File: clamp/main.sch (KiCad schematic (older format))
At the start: 36 parts, among them P1 CONN_01X12, U1 LM741, U2 LM741, U3 LM741, U4 LM741, U5 LM741, U6 LM741

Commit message: update
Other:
- moved on the sheet: R3, R4, R5
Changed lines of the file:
@@
 	4750 2250 4900 2250
+Wire Wire Line
+	4250 1850 4250 2050
 Wire Wire Line
 	4050 2050 4900 2050
@@
 Text GLabel 7550 4500 0    60   Input ~ 0
 -VE
-Text GLabel 1550 2050 0    60   Input ~ 0
+Text GLabel 1550 1850 0    60   Input ~ 0
 I-FB
 Text GLabel 1500 1500 0    60   Input ~ 0
 REF
-Text GLabel 1550 2250 0    60   Input ~ 0
+Text GLabel 1550 2050 0    60   Input ~ 0
 I-SET
 $Comp
 L R R3
 U 1 1 5807AAE8
+P 3900 1850
+F 0 "R3" V 3980 1850 50  0000 C CNN
+F 1 "R" V 3900 1850 50  0000 C CNN
+F 2 "Resistors_SMD:R_1206" V 3830 1850 50  0001 C CNN
+F 3 "" H 3900 1850 50  0000 C CNN
+	1    3900 1850
+	0    1    1    0
+$EndComp
+$Comp
+L R R4
+U 1 1 5807AB49
 P 3900 2050
-F 0 "R3" V 3980 2050 50  0000 C CNN
+F 0 "R4" V 3980 2050 50  0000 C CNN
 F 1 "R" V 3900 2050 50  0000 C CNN
 F 2 "Resistors_SMD:R_1206" V 3830 2050 50  0001 C CNN
@@
 	0    1    1    0
 $EndComp
-$Comp
-L R R4
-U 1 1 5807AB49
-P 3900 2250
-F 0 "R4" V 3980 2250 50  0000 C CNN
-F 1 "R" V 3900 2250 50  0000 C CNN
-F 2 "Resistors_SMD:R_1206" V 3830 2250 50  0001 C CNN
-F 3 "" H 3900 2250 50  0000 C CNN
-	1    3900 2250
-	0    1    1    0
-$EndComp
+Wire Wire Line
+	1550 1850 3750 1850
 Wire Wire Line
 	1550 2050 3750 2050
-Wire Wire Line
-	1550 2250 3750 2250
-Wire Wire Line
-	4050 2250 4250 2250
-Wire Wire Line
-	4250 2250 4250 2050
 Connection ~ 4250 2050
 Wire Wire Line
 	1950 3450 2150 3450
 Wire Wire Line
-	1950 2250 1950 3450
+	1950 2050 1950 3450
 $Comp
 L R R6
@@
 L R R5
 U 1 1 5807B7C8
-P 3950 3100
-F 0 "R5" V 4030 3100 50  0000 C CNN
-F 1 "R" V 3950 3100 50  0000 C CNN
-F 2 "Resistors_SMD:R_1206" V 3880 3100 50  0001 C CNN
-F 3 "" H 3950 3100 50  0000 C CNN
-	1    3950 3100
-	0    1    1    0
-$EndComp
-Connection ~ 1950 2250
-Wire Wire Line
-	3650 2050 3650 3100
-Wire Wire Line
-	3650 3100 3800 3100
-Connection ~ 3650 2050
-Wire Wire Line
-	4100 3100 4250 3100
-Wire Wire Line
-	4250 3100 4250 3350
+P 3950 3550
+F 0 "R5" V 4030 3550 50  0000 C CNN
+F 1 "R" V 3950 3550 50  0000 C CNN
+F 2 "Resistors_SMD:R_1206" V 3880 3550 50  0001 C CNN
+F 3 "" H 3950 3550 50  0000 C CNN
+	1    3950 3550
+	0    1    1    0
+$EndComp
+Connection ~ 1950 2050
+Wire Wire Line
+	4100 3550 4250 3550
+Wire Wire Line
+	4250 3550 4250 3350
 Wire Wire Line
 	4100 3350 4900 3350
@@
 F1 "test.sch" 60
 $EndSheet
+Wire Wire Line
+	4250 1850 4050 1850
+Wire Wire Line
+	3800 3550 3700 3550
+Wire Wire Line
+	3700 3550 3700 4350
+Wire Wire Line
+	3700 4350 1800 4350
+Wire Wire Line
+	1800 4350 1800 1850
+Connection ~ 1800 1850
 $EndSCHEMATC

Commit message: update
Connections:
- wire segments 74 -> 106
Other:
- moved on the sheet: R1, R2, U2
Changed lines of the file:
@@
 	4250 1850 4250 2050
 Wire Wire Line
-	4050 2050 4900 2050
+	4050 2050 4250 2050
+Wire Wire Line
+	4250 2050 4900 2050
 Wire Wire Line
 	5950 2150 6350 2150
@@
 	5950 1500 6350 1500
 Wire Wire Line
-	6350 1500 6350 6050
+	6350 1500 6350 2150
+Wire Wire Line
+	6350 2150 6350 2800
+Wire Wire Line
+	6350 2800 6350 3450
+Wire Wire Line
+	6350 3450 6350 4750
+Wire Wire Line
+	6350 4750 6350 5400
+Wire Wire Line
+	6350 5400 6350 6050
 Wire Wire Line
 	1500 1500 5650 1500
 Wire Wire Line
-	4750 2250 4750 3550
+	4750 2250 4750 2800
+Wire Wire Line
+	4750 2800 4750 3550
 Wire Wire Line
 	6350 2800 4750 2800
@@
 Connection ~ 4750 2800
 Wire Wire Line
-	3200 3350 3800 3350
+	10350 1900 10450 1900
+Wire Wire Line
+	10450 1900 10950 1900
 Text GLabel 5100 3150 1    60   Input ~ 0
 +VE
@@
 	5500 3450 5700 3450
 Wire Wire Line
-	6000 3450 6600 3450
+	6000 3450 6350 3450
+Wire Wire Line
+	6350 3450 6600 3450
 Connection ~ 6350 2800
 $Comp
 L LM741 U2
 U 1 1 58079399
-P 2900 3350
-F 0 "U2" H 2900 3600 50  0000 L CNN
-F 1 "LM741" H 2900 3500 50  0000 L CNN
-F 2 "Housings_SOIC:SOIC-8_3.9x4.9mm_Pitch1.27mm" H 2950 3400 50  0001 C CNN
-F 3 "" H 3050 3500 50  0000 C CNN
-	1    2900 3350
-	1    0    0    -1
-$EndComp
-Wire Wire Line
-	2350 3250 2600 3250
-Wire Wire Line
-	3300 3350 3300 4000
-Wire Wire Line
-	3300 4000 3000 4000
+P 10050 1900
+F 0 "U2" H 10050 2150 50  0000 L CNN
+F 1 "LM741" H 10050 2050 50  0000 L CNN
+F 2 "Housings_SOIC:SOIC-8_3.9x4.9mm_Pitch1.27mm" H 10100 1950 50  0001 C CNN
+F 3 "" H 10200 2050 50  0000 C CNN
+	1    10050 1900
+	1    0    0    -1
+$EndComp
+Wire Wire Line
+	9500 1800 9750 1800
+Wire Wire Line
+	10450 1900 10450 2550
+Wire Wire Line
+	10450 2550 10150 2550
 $Comp
 L R R2
 U 1 1 580795D9
-P 2850 4000
-F 0 "R2" V 2930 4000 50  0000 C CNN
-F 1 "R" V 2850 4000 50  0000 C CNN
-F 2 "Resistors_SMD:R_1206" V 2780 4000 50  0001 C CNN
-F 3 "" H 2850 4000 50  0000 C CNN
-	1    2850 4000
+P 10000 2550
+F 0 "R2" V 10080 2550 50  0000 C CNN
+F 1 "R" V 10000 2550 50  0000 C CNN
+F 2 "Resistors_SMD:R_1206" V 9930 2550 50  0001 C CNN
+F 3 "" H 10000 2550 50  0000 C CNN
+	1    10000 2550
 	0    1    1    0
 $EndComp
@@
 L R R1
 U 1 1 58079640
-P 2300 3450
-F 0 "R1" V 2380 3450 50  0000 C CNN
-F 1 "R" V 2300 3450 50  0000 C CNN
-F 2 "Resistors_SMD:R_1206" V 2230 3450 50  0001 C CNN
-F 3 "" H 2300 3450 50  0000 C CNN
-	1    2300 3450
-	0    1    1    0
-$EndComp
-Wire Wire Line
-	2450 3450 2600 3450
-Wire Wire Line
-	2500 3450 2500 4000
-Wire Wire Line
-	2500 4000 2700 4000
-Connection ~ 2500 3450
-Text GLabel 2800 3050 1    60   Input ~ 0
+P 9450 2000
+F 0 "R1" V 9530 2000 50  0000 C CNN
+F 1 "R" V 9450 2000 50  0000 C CNN
+F 2 "Resistors_SMD:R_1206" V 9380 2000 50  0001 C CNN
+F 3 "" H 9450 2000 50  0000 C CNN
+	1    9450 2000
+	0    1    1    0
+$EndComp
+Wire Wire Line
+	9600 2000 9650 2000
+Wire Wire Line
+	9650 2000 9750 2000
+Wire Wire Line
+	9650 2000 9650 2550
+Wire Wire Line
+	9650 2550 9850 2550
+Connection ~ 9650 2000
+Text GLabel 9950 1600 1    60   Input ~ 0
 +VE
-Text GLabel 2800 3650 3    60   Input ~ 0
+Text GLabel 9950 2200 3    60   Input ~ 0
 -VE
-NoConn ~ 2900 3650
-NoConn ~ 3000 3650
-Connection ~ 3300 3350
+NoConn ~ 10050 2200
+NoConn ~ 10150 2200
+Connection ~ 10450 1900
 Text GLabel 5100 1850 1    60   Input ~ 0
 +VE
 Wire Notes Line
-	2150 2750 2150 4150
+	9300 1300 9300 2700
 Wire Notes Line
-	2150 4150 3450 4150
+	9300 2700 10600 2700
 Wire Notes Line
-	3450 2750 2150 2750
+	10600 1300 9300 1300
 Text GLabel 7550 4500 0    60   Input ~ 0
 -VE
@@
 $EndComp
 Wire Wire Line
-	1550 1850 3750 1850
-Wire Wire Line
-	1550 2050 3750 2050
+	1550 1850 1800 1850
+Wire Wire Line
+	1800 1850 3750 1850
+Wire Wire Line
+	1550 2050 1950 2050
+Wire Wire Line
+	1950 2050 3750 2050
 Connection ~ 4250 2050
 Wire Wire Line
-	1950 3450 2150 3450
+	9100 2000 9300 2000
 Wire Wire Line
 	1950 2050 1950 3450
@@
 	4250 3550 4250 3350
 Wire Wire Line
-	4100 3350 4900 3350
+	4100 3350 4250 3350
+Wire Wire Line
+	4250 3350 4900 3350
 Connection ~ 4250 3350
 Wire Notes Line
-	3450 4150 3450 2750
+	10600 2700 10600 1300
 Text GLabel 7550 4900 0    60   Input ~ 0
 I-SET
@@
 	7000 1700 7000 1800
 Wire Wire Line
-	7000 1800 8700 1800
+	7000 1800 7200 1800
+Wire Wire Line
+	7200 1800 7450 1800
+Wire Wire Line
+	7450 1800 7700 1800
+Wire Wire Line
+	7700 1800 7950 1800
+Wire Wire Line
+	7950 1800 8200 1800
+Wire Wire Line
+	8200 1800 8450 1800
+Wire Wire Line
+	8450 1800 8700 1800
 Connection ~ 7200 1800
 Text GLabel 7200 2100 3    60   Input ~ 0
@@
 	7000 2950 7000 3050
 Wire Wire Line
-	7000 3050 8700 3050
+	7000 3050 7200 3050
+Wire Wire Line
+	7200 3050 7450 3050
+Wire Wire Line
+	7450 3050 7700 3050
+Wire Wire Line
+	7700 3050 7950 3050
+Wire Wire Line
+	7950 3050 8200 3050
+Wire Wire Line
+	8200 3050 8450 3050
+Wire Wire Line
+	8450 3050 8700 3050
 Connection ~ 7200 3050
 Text GLabel 7200 3350 3    60   Input ~ 0
@@
 NoConn ~ 7850 5450
 NoConn ~ 7850 5400
-Text GLabel 2350 3050 1    60   Input ~ 0
-GND
-Wire Wire Line
-	2350 3050 2350 3250
+Text GLabel 9500 1600 1    60   Input ~ 0
+GND
+Wire Wire Line
+	9500 1600 9500 1800
 $Comp
 L LM741 U5
@@
 	4750 4850 4900 4850
 Wire Wire Line
-	4050 4650 4900 4650
+	4050 4650 4250 4650
+Wire Wire Line
+	4250 4650 4900 4650
 Wire Wire Line
 	6350 4750 5950 4750
 Wire Wire Line
-	4750 4850 4750 6150
+	4750 4850 4750 5400
+Wire Wire Line
+	4750 5400 4750 6150
 Wire Wire Line
 	6350 5400 4750 5400
@@
 Connection ~ 4750 5400
 Wire Wire Line
-	3200 5950 3800 5950
+	3200 5950 3300 5950
+Wire Wire Line
+	3300 5950 3800 5950
 Text GLabel 5100 5750 1    60   Input ~ 0
 +VE
@@
 $EndComp
 Wire Wire Line
-	2450 6050 2600 6050
+	2450 6050 2500 6050
+Wire Wire Line
+	2500 6050 2600 6050
 Wire Wire Line
 	2500 6050 2500 6600
@@
 $EndComp
 Wire Wire Line
-	1550 4650 3750 4650
-Wire Wire Line
-	1550 4850 3750 4850
+	1550 4650 3650 4650
+Wire Wire Line
+	3650 4650 3750 4650
+Wire Wire Line
+	1550 4850 1950 4850
+Wire Wire Line
+	1950 4850 3750 4850
 Wire Wire Line
 	4050 4850 4250 4850
@@
 	4250 5700 4250 5950
 Wire Wire Line
-	4100 5950 4900 5950
+	4100 5950 4250 5950
+Wire Wire Line
+	4250 5950 4900 5950
 Connection ~ 4250 5950
 Wire Notes Line
@@
 	7850 5200 7550 5200
 NoConn ~ 7850 5500
+Wire Wire Line
+	4250 1850 4050 1850
+Wire Wire Line
+	3800 3550 3700 3550
+Wire Wire Line
+	3700 3550 3700 4350
+Wire Wire Line
+	3700 4350 1800 4350
+Wire Wire Line
+	1800 4350 1800 1850
+Connection ~ 1800 1850
+Text GLabel 9150 4150 3    60   Input ~ 0
+GND
 $Sheet
-S 9350 2050 1300 1000
-U 580BA788
+S 9450 3100 1300 1000
+U 585BBA35
 F0 "test" 60
 F1 "test.sch" 60
 $EndSheet
-Wire Wire Line
-	4250 1850 4050 1850
-Wire Wire Line
-	3800 3550 3700 3550
-Wire Wire Line
-	3700 3550 3700 4350
-Wire Wire Line
-	3700 4350 1800 4350
-Wire Wire Line
-	1800 4350 1800 1850
-Connection ~ 1800 1850
 $EndSCHEMATC

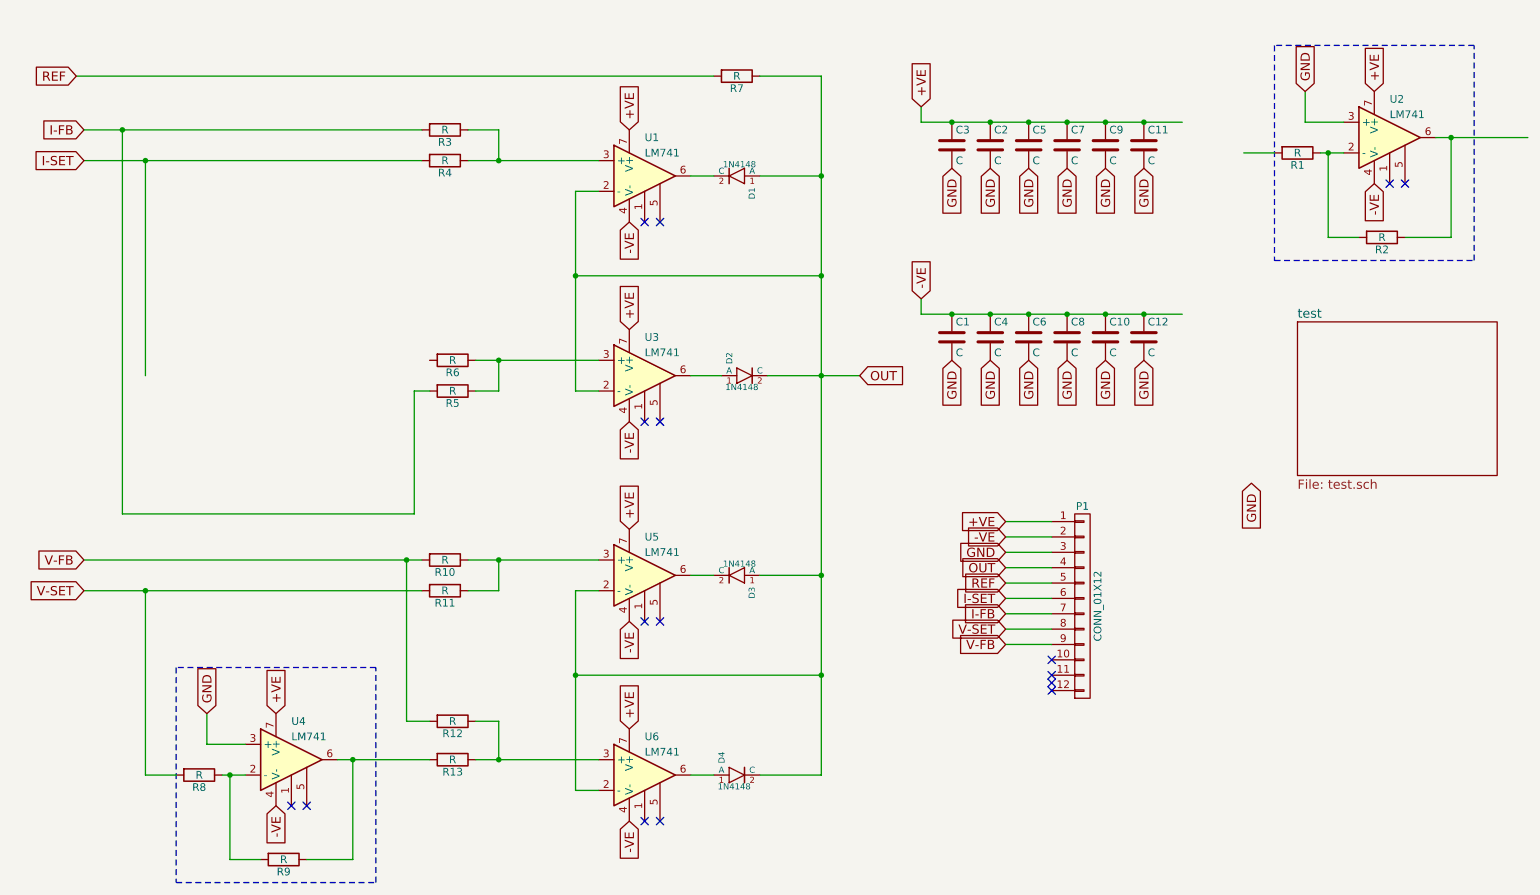
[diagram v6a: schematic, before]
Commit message: add ADC
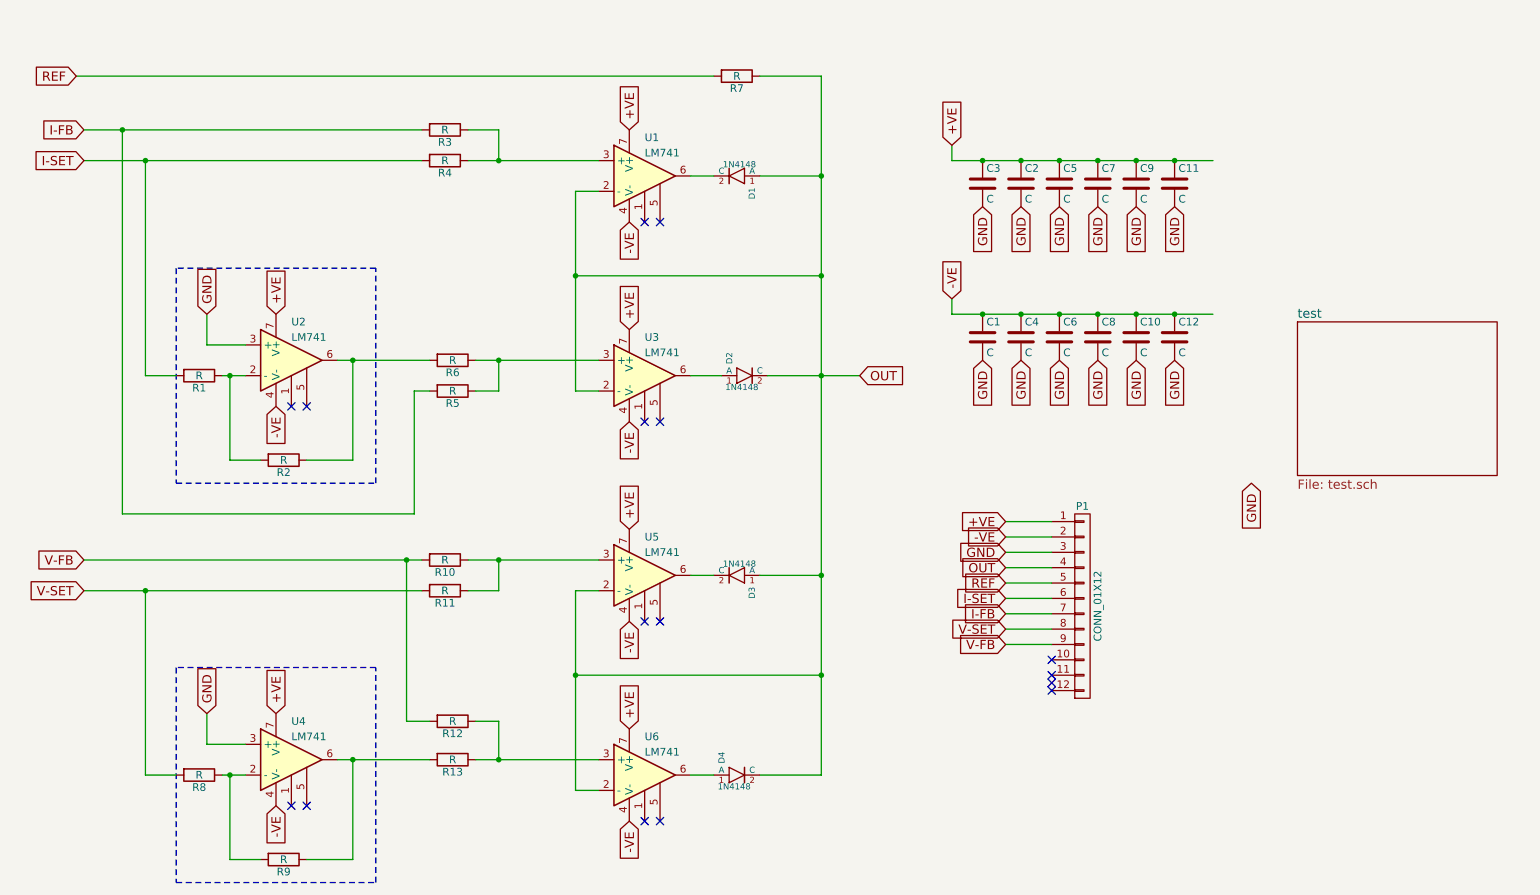
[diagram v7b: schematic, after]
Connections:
- wire segments 106 -> 74
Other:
- moved on the sheet: C1, C10, C11, C12, C2, C3, C4, C5, C6, C7, C8, C9

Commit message: move clamps
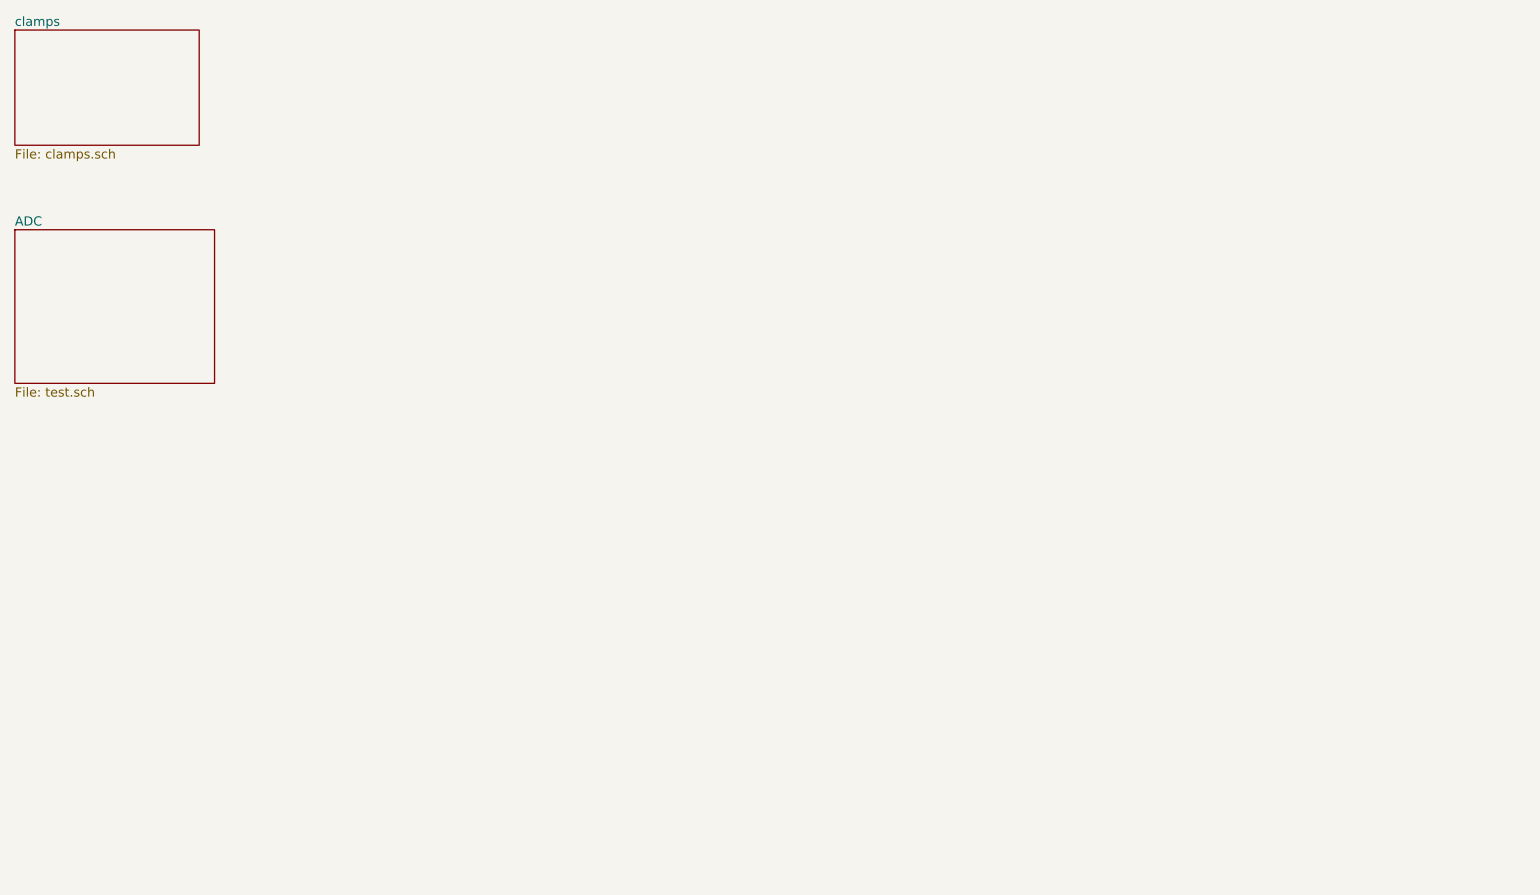
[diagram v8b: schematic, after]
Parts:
- removed C1, C10, C11, C12, C2, C3, C4, C5, C6, C7, C8, C9: C, Capacitors_SMD:C_1206, symbol C
- removed D1, D2, D3, D4: 1N4148, Diodes_SMD:MiniMELF_Standard, symbol 1N4148
- removed P1: CONN_01X12, Pin_Headers:Pin_Header_Straight_1x12, symbol CONN_01X12
- removed R1, R10, R11, R12, R13, R2, R3, R4, R5, R6, R7, R8, R9: R, Resistors_SMD:R_1206, symbol R
- removed U1, U2, U3, U4, U5, U6: LM741, Housings_SOIC:SOIC-8_3.9x4.9mm_Pitch1.27mm, symbol LM741
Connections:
- no-connect marks 16 -> 0
